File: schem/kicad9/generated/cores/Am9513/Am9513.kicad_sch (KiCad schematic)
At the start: 0 parts

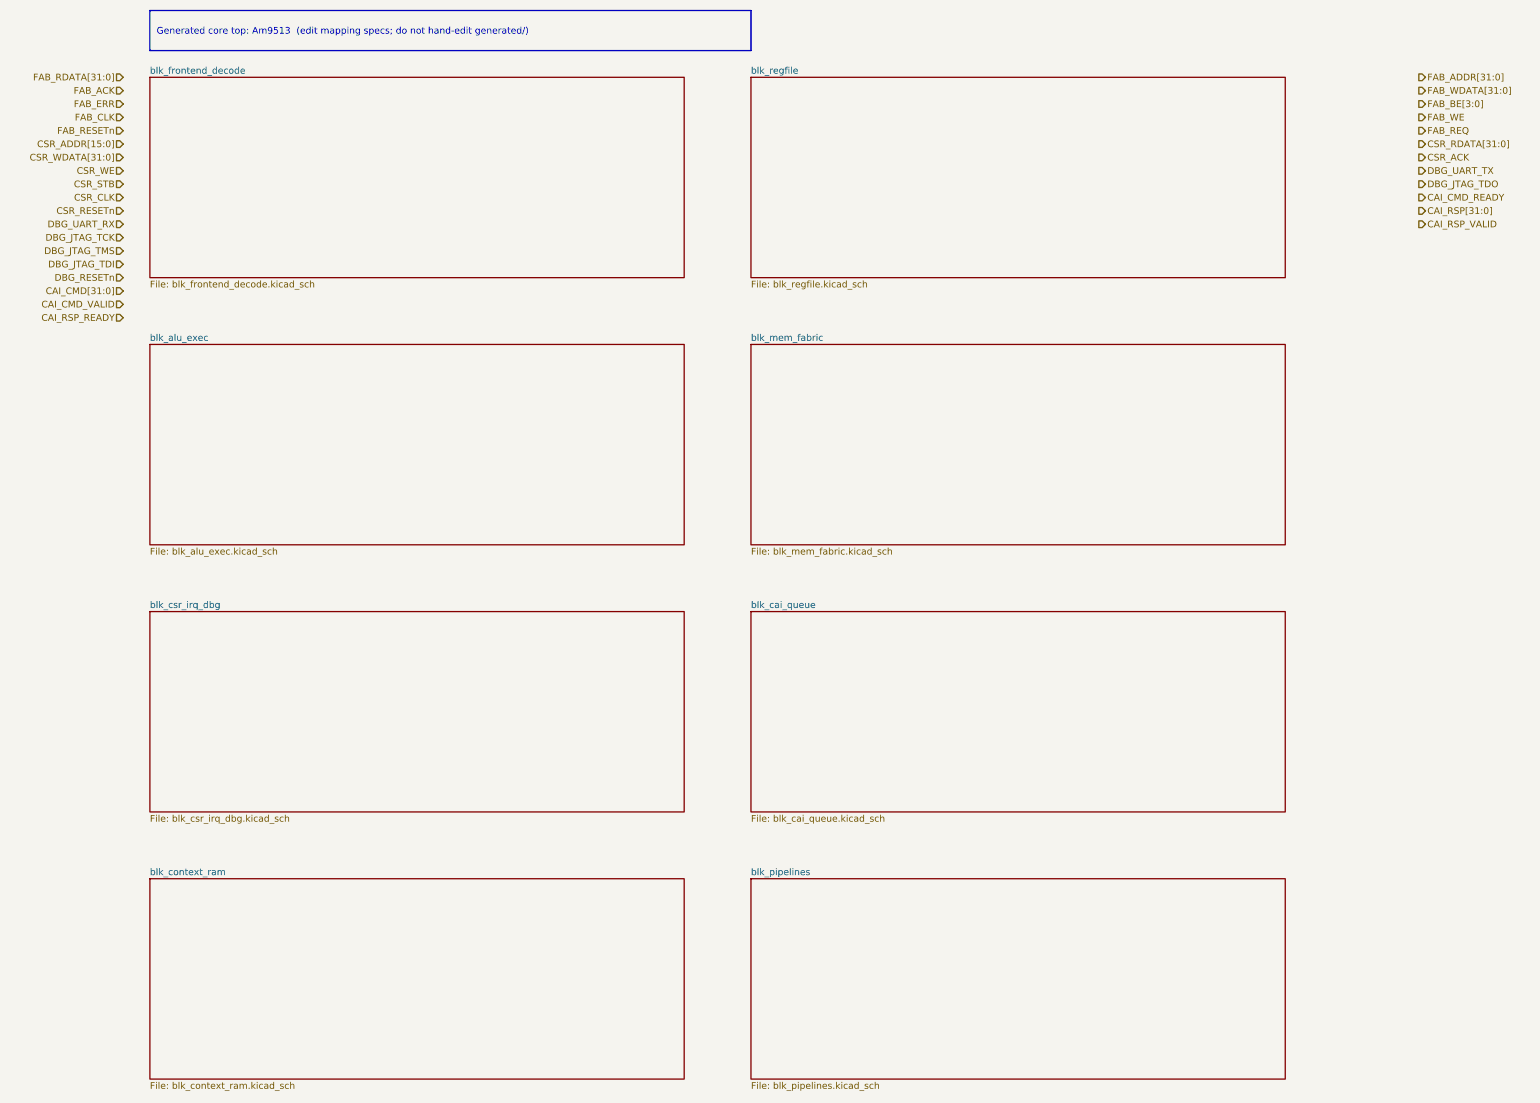
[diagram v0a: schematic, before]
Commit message: kicad: generate core-level hierarchical schematics
Detailed description:
- What changed: regenerated common and core schematics for Z85/Z90/Z380/Z480, Am9513/4/5, Am95xx, and CarbonIO/DMA placeholders
- Why it changed: update generated KiCad 9 outputs to reflect the final naming and tier model
- Files/paths affected: schem/kicad9/generated/common/* and schem/kicad9/generated/cores/*
- How to run it: scripts/gen_kicad.sh (or python tools/kicadgen/src/kicadgen.py)
- What remains TODO: regenerate and commit system-level schematics
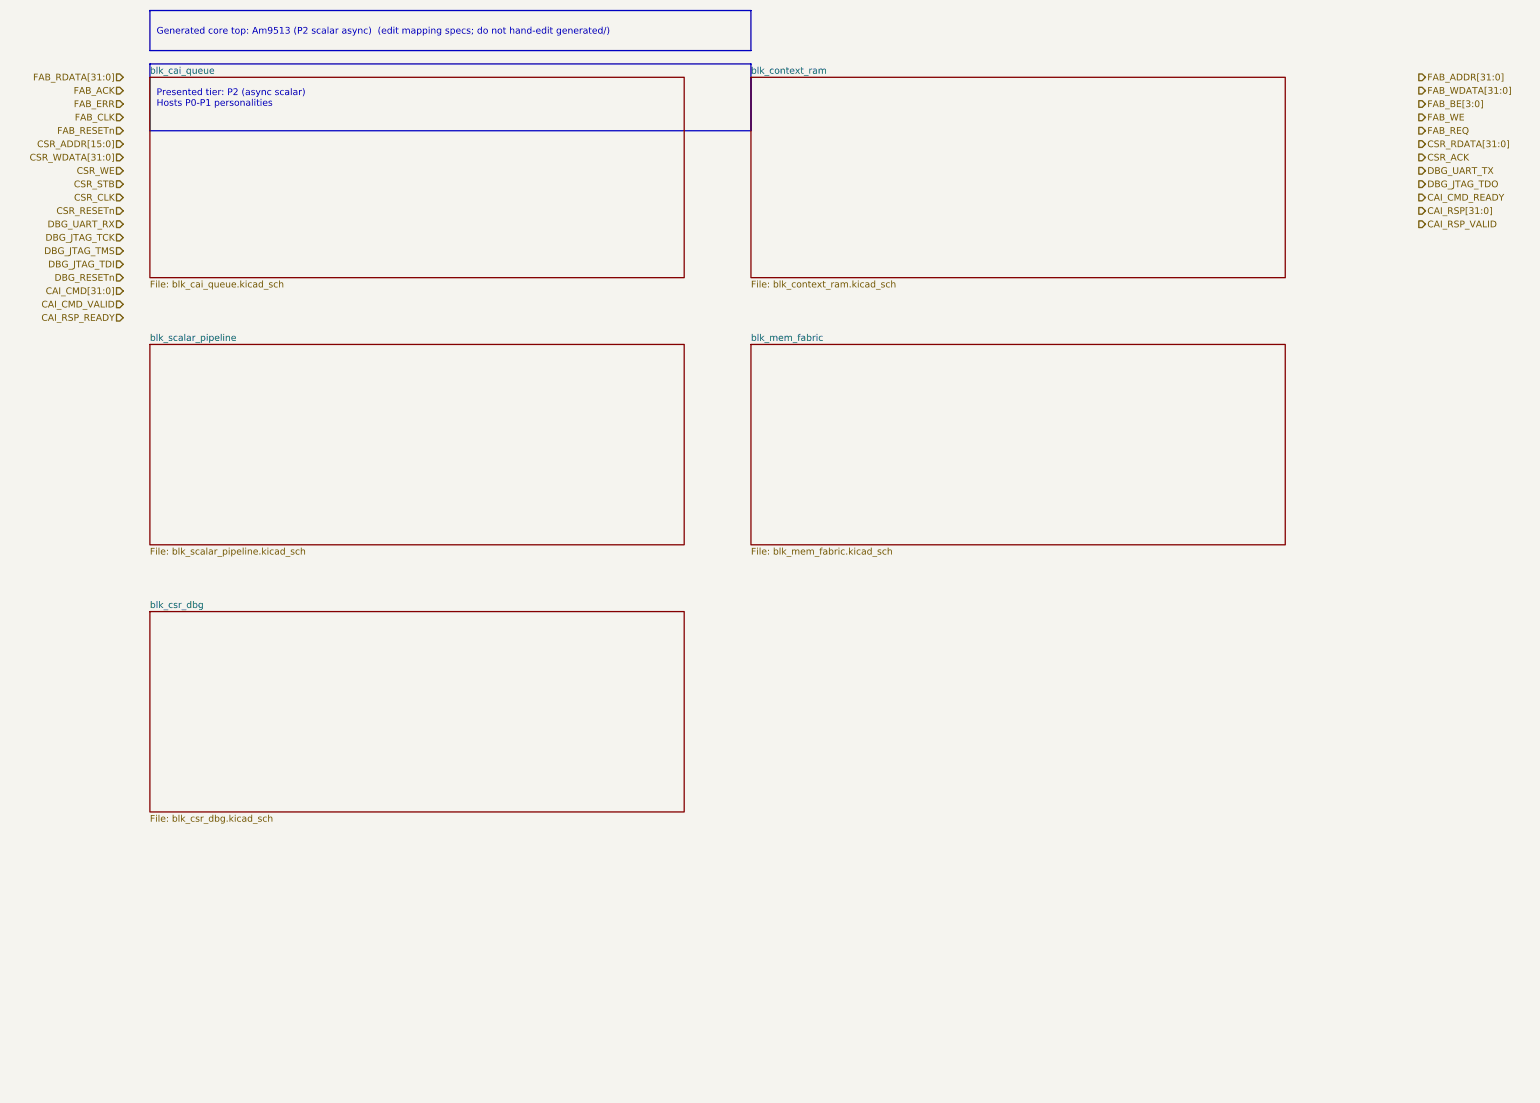
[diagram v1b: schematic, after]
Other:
- removed sheet blk_alu_exec
- removed sheet blk_csr_irq_dbg
- removed sheet blk_frontend_decode
- removed sheet blk_pipelines
- removed sheet blk_regfile
- added sheet blk_csr_dbg (blk_csr_dbg.kicad_sch)
- added sheet blk_scalar_pipeline (blk_scalar_pipeline.kicad_sch)
- title: Am9513 (generated) -> Am9513 (P2 scalar async) (generated)
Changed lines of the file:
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@@
 	(version 20250114)
 	(generator "kicadgen")
-	(generator_version "0.1")
+	(generator_version "0.2")
 	(paper "A3")
 	(title_block
-		(title "Am9513 (generated)")
+		(title "Am9513 (P2 scalar async) (generated)")
 		(company "Project Carbon")
 		(comment 1 "Generated - do not edit in generated/")
@@
 	)
 	(text_box
-		"Generated core top: Am9513  (edit mapping specs; do not hand-edit generated/)"
+		"Generated core top: Am9513 (P2 scalar async)  (edit mapping specs; do not hand-edit generated/)"
 		(exclude_from_sim no)
 		(at
@@
 		)
 	)
+	(text_box
+		"Presented tier: P2 (async scalar)\nHosts P0-P1 personalities"
+		(exclude_from_sim no)
+		(at
+			12.7
+			22.86
+			0
+		)
+		(size 114.3 12.7)
+		(margins
+			1.27
+			1.27
+			1.27
+			1.27
+		)
+		(stroke
+			(width 0)
+			(type default)
+			(color
+				0
+				0
+				0
+				1
+			)
+		)
+		(fill
+			(type color)
+			(color
+				255
+				255
+				150
+				1
+			)
+		)
+		(effects
+			(font
+				(size 1.27 1.27)
+			)
+			(justify left)
+		)
+	)
 	(sheet
 		(at 12.7 25.4)
@@
 		(property
 			"Sheetname"
-			"blk_frontend_decode"
+			"blk_cai_queue"
 			(at
 				12.7
@@
 		(property
 			"Sheetfile"
-			"blk_frontend_decode.kicad_sch"
+			"blk_cai_queue.kicad_sch"
 			(at
 				12.7
@@
 		(property
 			"Sheetname"
-			"blk_regfile"
+			"blk_context_ram"
 			(at
 				127
@@
 		(property
 			"Sheetfile"
-			"blk_regfile.kicad_sch"
+			"blk_context_ram.kicad_sch"
 			(at
 				127
@@
 		(property
 			"Sheetname"
-			"blk_alu_exec"
+			"blk_scalar_pipeline"
 			(at
 				12.7
@@
 		(property
 			"Sheetfile"
-			"blk_alu_exec.kicad_sch"
+			"blk_scalar_pipeline.kicad_sch"
 			(at
 				12.7
@@
 		(property
 			"Sheetname"
-			"blk_csr_irq_dbg"
+			"blk_csr_dbg"
 			(at
 				12.7
@@
 		(property
 			"Sheetfile"
-			"blk_csr_irq_dbg.kicad_sch"
+			"blk_csr_dbg.kicad_sch"
 			(at
 				12.7
@@
 				)
 			)
-		)
-	)
-	(sheet
-		(at 127 127)
-		(size 101.6 38.1)
-		(exclude_from_sim no)
-		(in_bom yes)
-		(on_board yes)
-		(dnp no)
-		(stroke
-			(width 0)
-			(type solid)
-		)
-		(fill
-			(color
-				0
-				0
-				0
-				0
-			)
-		)
-		(property
-			"Sheetname"
-			"blk_cai_queue"
-			(at
-				127
-				125.73
-				0
-			)
-			(effects
-				(font
-					(size 1.27 1.27)
-				)
-				(justify left)
-			)
-		)
-		(property
-			"Sheetfile"
-			"blk_cai_queue.kicad_sch"
-			(at
-				127
-				166.37
-				0
-			)
-			(effects
-				(font
-					(size 1.27 1.27)
-				)
-				(justify left)
-			)
-		)
-		(instances
-			(project
-				"core_Am9513"
-				(path
-					"/92267c30-7a9b-5a25-8278-1a73dfaaf2f0"
-					(page "7")
-				)
-			)
-		)
-	)
-	(sheet
-		(at 12.7 177.8)
-		(size 101.6 38.1)
-		(exclude_from_sim no)
-		(in_bom yes)
-		(on_board yes)
-		(dnp no)
-		(stroke
-			(width 0)
-			(type solid)
-		)
-		(fill
-			(color
-				0
-				0
-				0
-				0
-			)
-		)
-		(property
-			"Sheetname"
-			"blk_context_ram"
-			(at
-				12.7
-				176.53
-				0
-			)
-			(effects
-				(font
-					(size 1.27 1.27)
-				)
-				(justify left)
-			)
-		)
-		(property
-			"Sheetfile"
-			"blk_context_ram.kicad_sch"
-			(at
-				12.7
-				217.17
-				0
-			)
-			(effects
-				(font
-					(size 1.27 1.27)
-				)
-				(justify left)
-			)
-		)
-		(instances
-			(project
-				"core_Am9513"
-				(path
-					"/92267c30-7a9b-5a25-8278-1a73dfaaf2f0"
-					(page "8")
-				)
-			)
-		)
-	)
-	(sheet
-		(at 127 177.8)
-		(size 101.6 38.1)
-		(exclude_from_sim no)
-		(in_bom yes)
-		(on_board yes)
-		(dnp no)
-		(stroke
-			(width 0)
-			(type solid)
-		)
-		(fill
-			(color
-				0
-				0
-				0
-				0
-			)
-		)
-		(property
-			"Sheetname"
-			"blk_pipelines"
-			(at
-				127
-				176.53
-				0
-			)
-			(effects
-				(font
-					(size 1.27 1.27)
-				)
-				(justify left)
-			)
-		)
-		(property
-			"Sheetfile"
-			"blk_pipelines.kicad_sch"
-			(at
-				127
-				217.17
-				0
-			)
-			(effects
-				(font
-					(size 1.27 1.27)
-				)
-				(justify left)
-			)
-		)
-		(instances
-			(project
-				"core_Am9513"
-				(path
-					"/92267c30-7a9b-5a25-8278-1a73dfaaf2f0"
-					(page "9")
-				)
-			)
